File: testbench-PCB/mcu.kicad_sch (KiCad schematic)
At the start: 18 parts, among them J2 AVR-ISP, J3 AVR-JTAG, SW1 SW_Push, U1 ATmega2561-16A, Y1 X322516MLB4SI

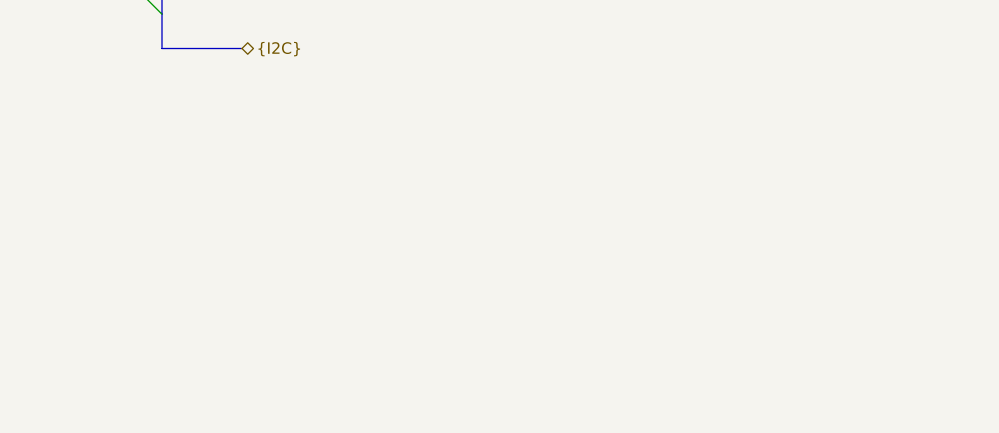
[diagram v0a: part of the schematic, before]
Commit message: Added titles to schematics.
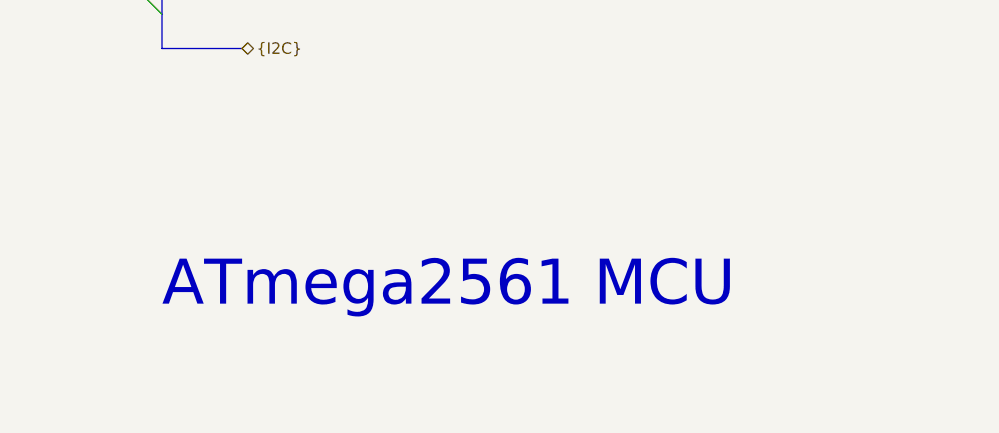
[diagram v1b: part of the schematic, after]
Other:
- note added: "ATmega2561 MCU"
- company: (none) -> Company: VUT Brno
- title: (none) -> Test benches for microcontroller kits
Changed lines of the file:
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@@
 (kicad_sch (version 20230121) (generator eeschema)
   (paper "A4")
+  (title_block
+    (title "Test benches for microcontroller kits")
+    (date "2023")
+    (rev "v0.1")
+    (company "Company: VUT Brno")
+    (comment 1 "Author: Ivo Zaludek")
+  )
   (bus_alias "UART1" (members "UART1_TXD" "UART1_RXD"))
   (junction (at 81.28 63.5) (diameter 0) (color 0 0 0 0)
@@
     (stroke (width 0) (type default))
   )
+  (text "ATmega2561 MCU" (at 177.8 173.99 0)
+    (effects (font (size 5 5)) (justify left bottom))
+  )
   (label "DUT_D3" (at 102.87 92.71 0) (fields_autoplaced)
